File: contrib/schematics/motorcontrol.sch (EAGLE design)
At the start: 27 parts, among them IC1 MEGA8-P, IC2 MAX 603, Q1 16 MHz

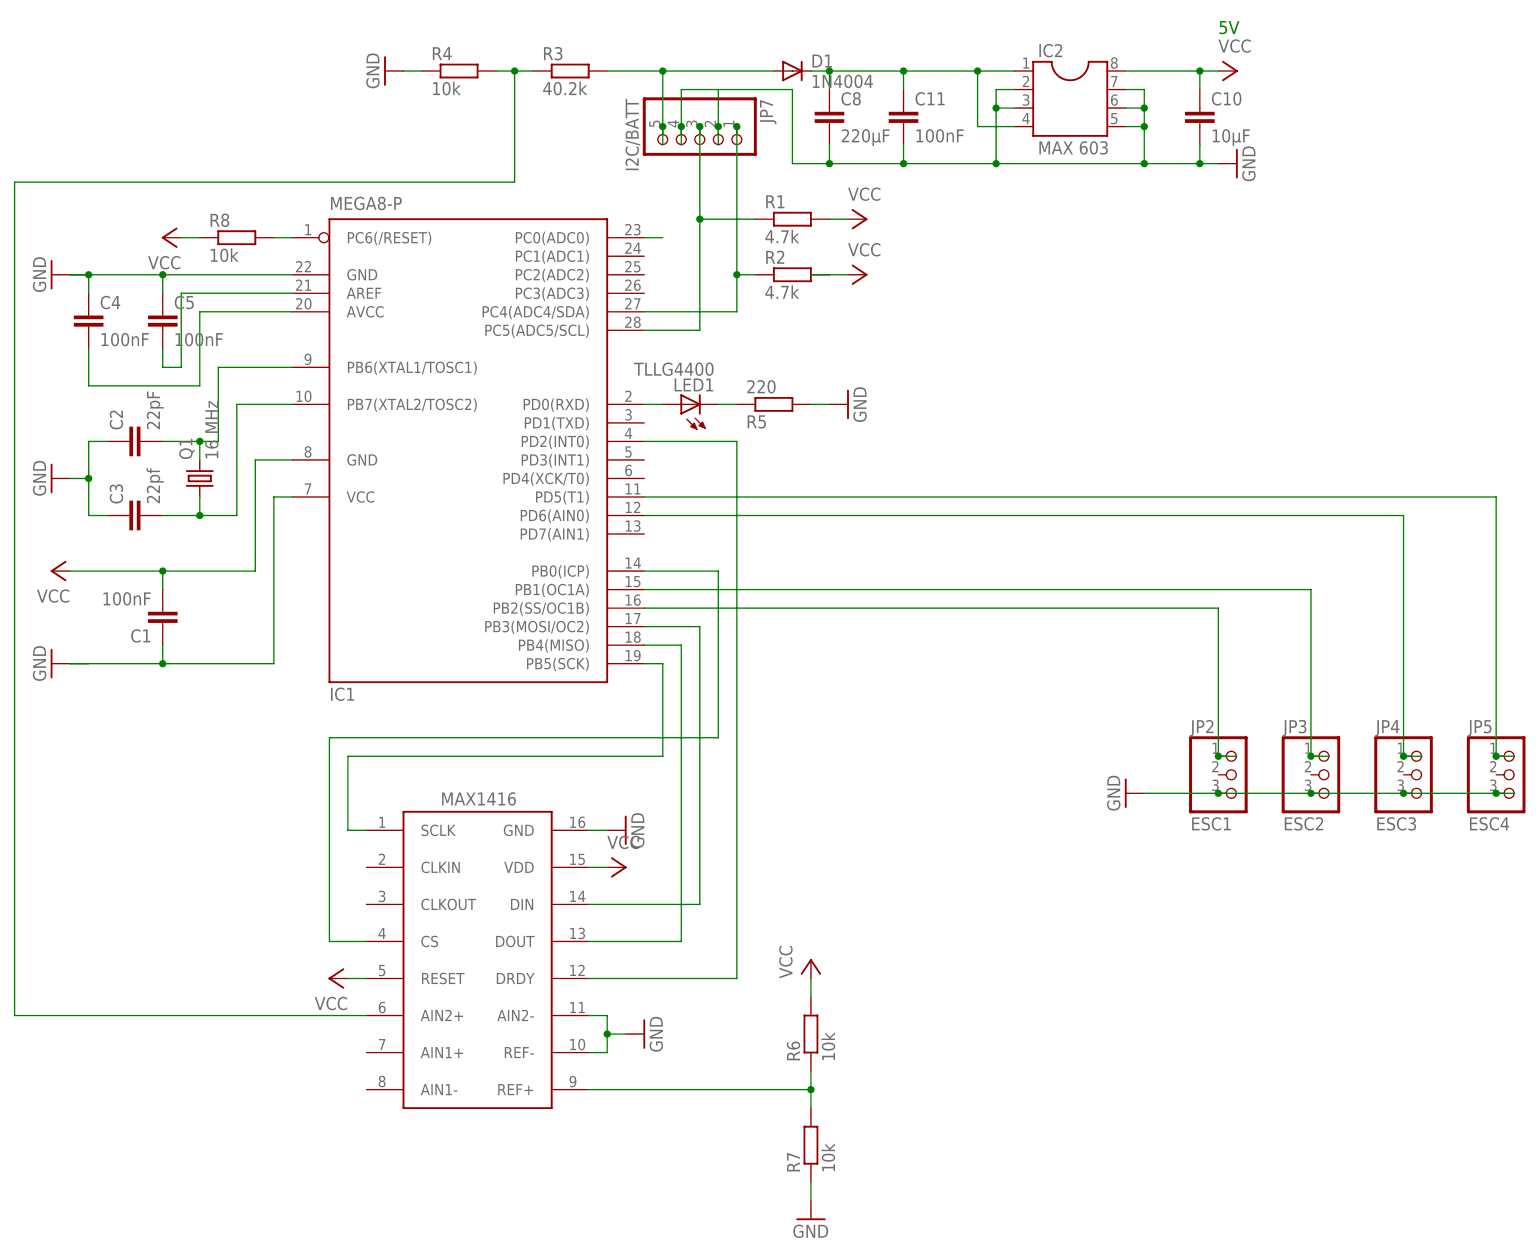
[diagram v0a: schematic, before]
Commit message: Updated motorcontrol schematics
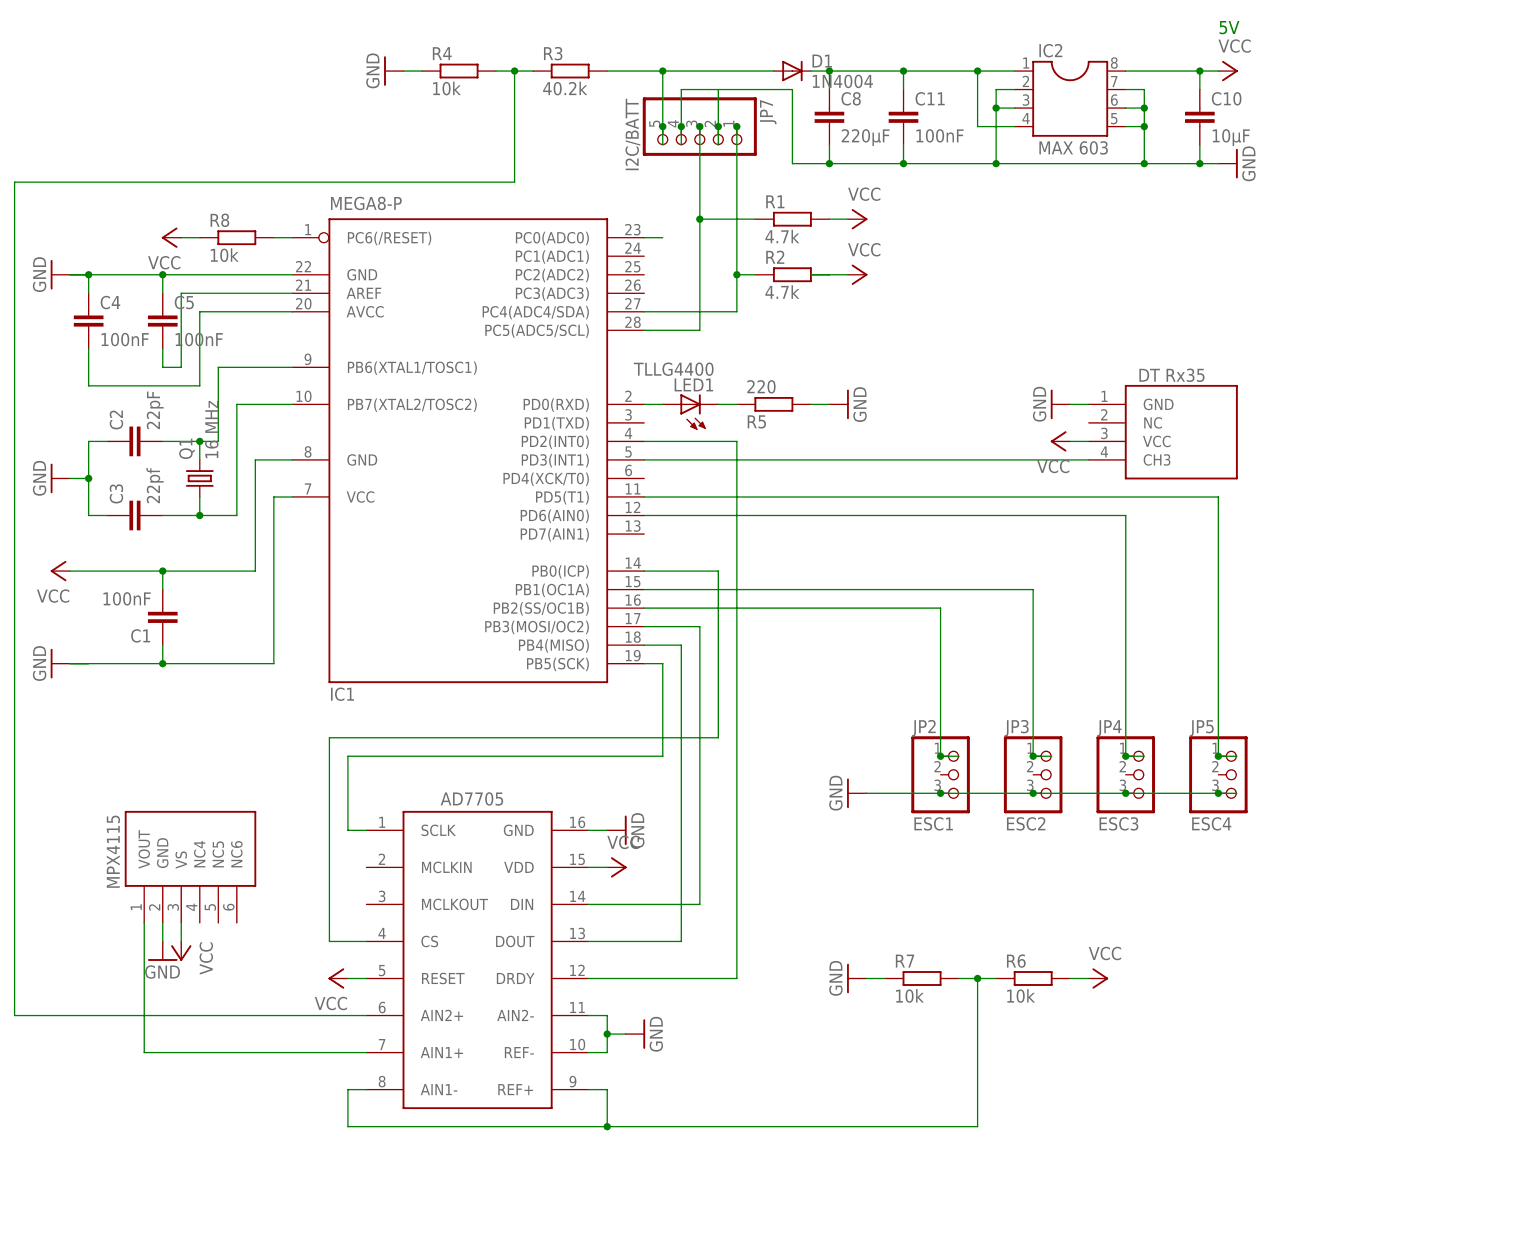
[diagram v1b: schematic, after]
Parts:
- added U$2: DTRX35, DTRX35:DTRX35
- added U$3: MPX4115, MPX4115:MPX4115
- U$1: value MAX1416 -> AD7705; device max1416:MAX1416 -> ad7705:AD7705
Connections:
- new net N$24: IC1.PD3(INT1), U$2.CH3
- new net N$25: U$1.AIN1+, U$3.VOUT
- net GND: now also U$2.GND, U$3.GND
- net N$22: now also U$1.AIN1-
- net VCC: now also U$2.VCC, U$3.VS
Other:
- moved on the sheet: JP2, JP3, JP4, JP5, R6, R7

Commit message: Implemented RX decoder in motorcontrol
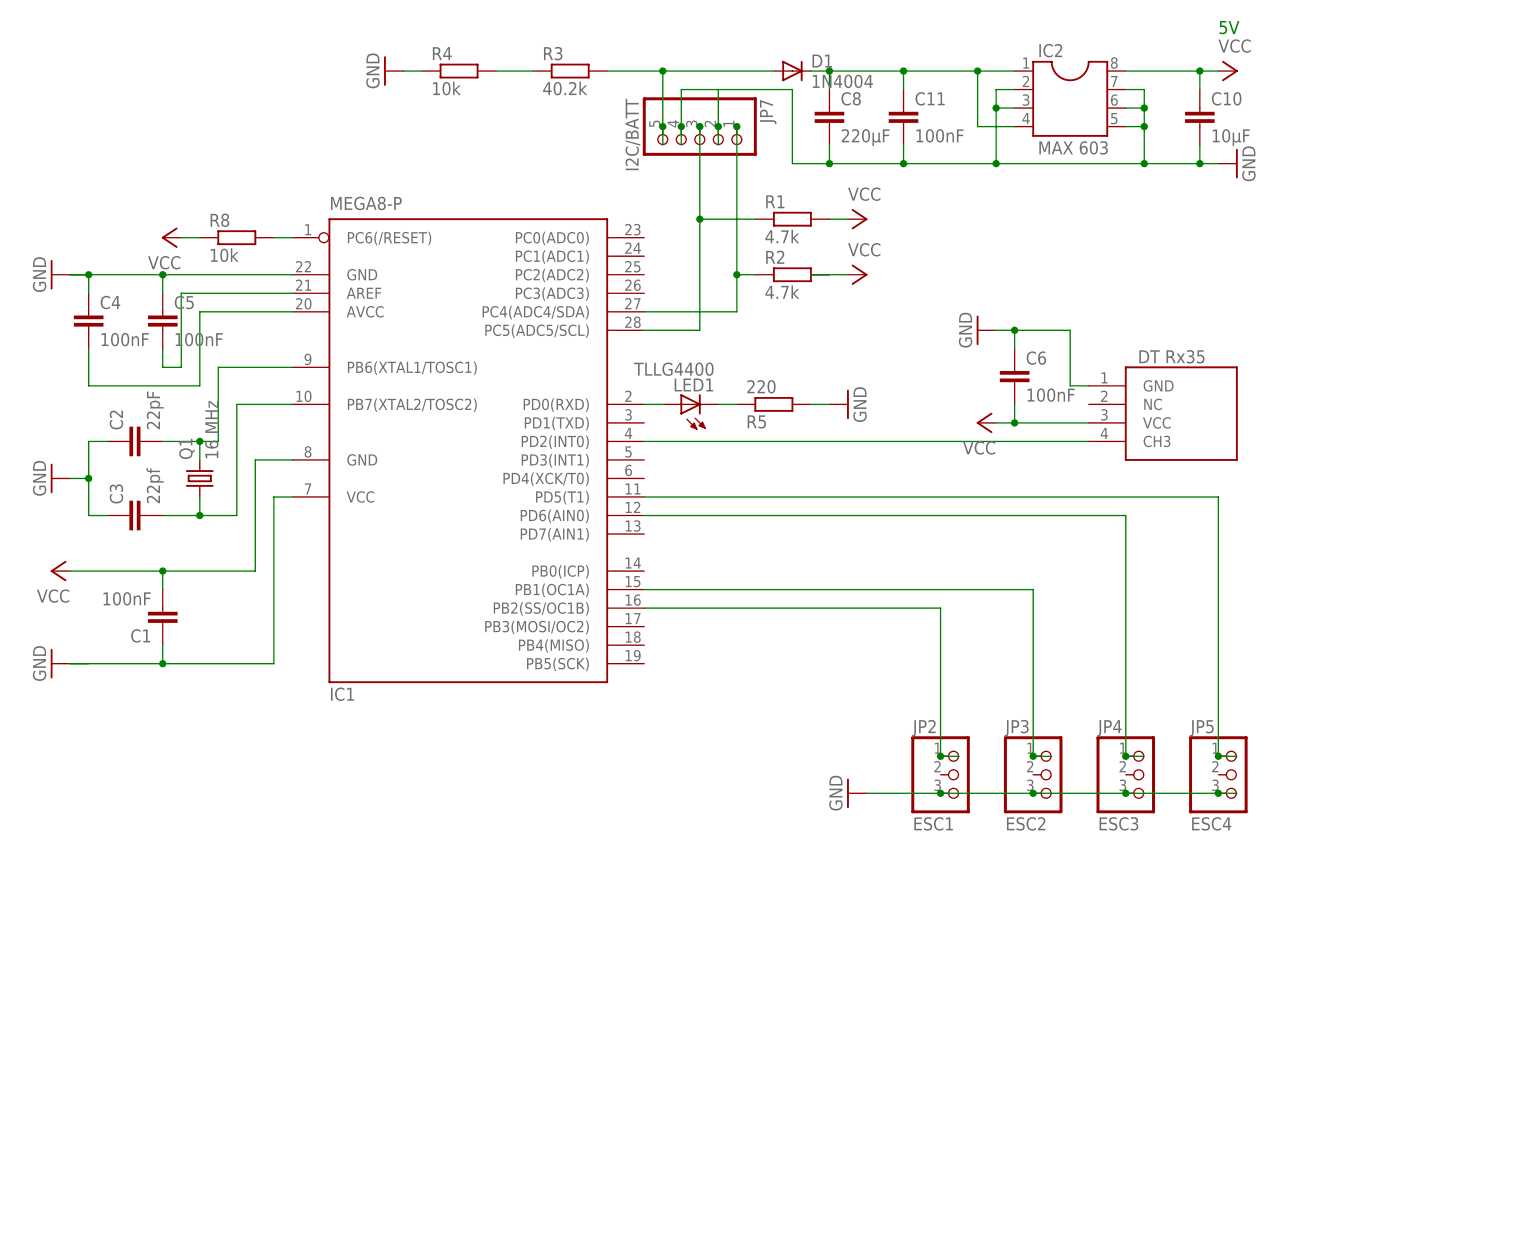
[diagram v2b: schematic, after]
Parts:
- removed R6, R7: 10k, resistor:R-EU_0207/2V
- removed U$1: AD7705, ad7705:AD7705
- removed U$3: MPX4115, MPX4115:MPX4115
- added C6: 100nF, capacitor-wima:C2.5/2
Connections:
- removed net N$15: IC1.PB4(MISO), U$1.DOUT
- removed net N$16: IC1.PB3(MOSI/OC2), U$1.DIN
- removed net N$17: IC1.PB5(SCK), U$1.SCLK
- removed net N$19: IC1.PB0(ICP), U$1.CS
- removed net N$20: IC1.PD2(INT0), U$1.DRDY
- removed net N$21: IC1.PC0(ADC0)
- removed net N$22: R6.1, R7.2, U$1.AIN1-, U$1.REF+
- removed net N$25: U$1.AIN1+, U$3.VOUT
- net GND: now also C6.1; no longer R7.1, U$1.AIN2-, U$1.GND, U$1.REF-, U$3.GND
- net N$13: no longer U$1.AIN2+
- net N$24: now also IC1.PD2(INT0); no longer IC1.PD3(INT1)
- net VCC: now also C6.2; no longer R6.2, U$1.RESET, U$1.VDD, U$3.VS
